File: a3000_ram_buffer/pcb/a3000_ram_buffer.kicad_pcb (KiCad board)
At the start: 2 copper layers, 167.6 x 43.2 mm, 29 parts

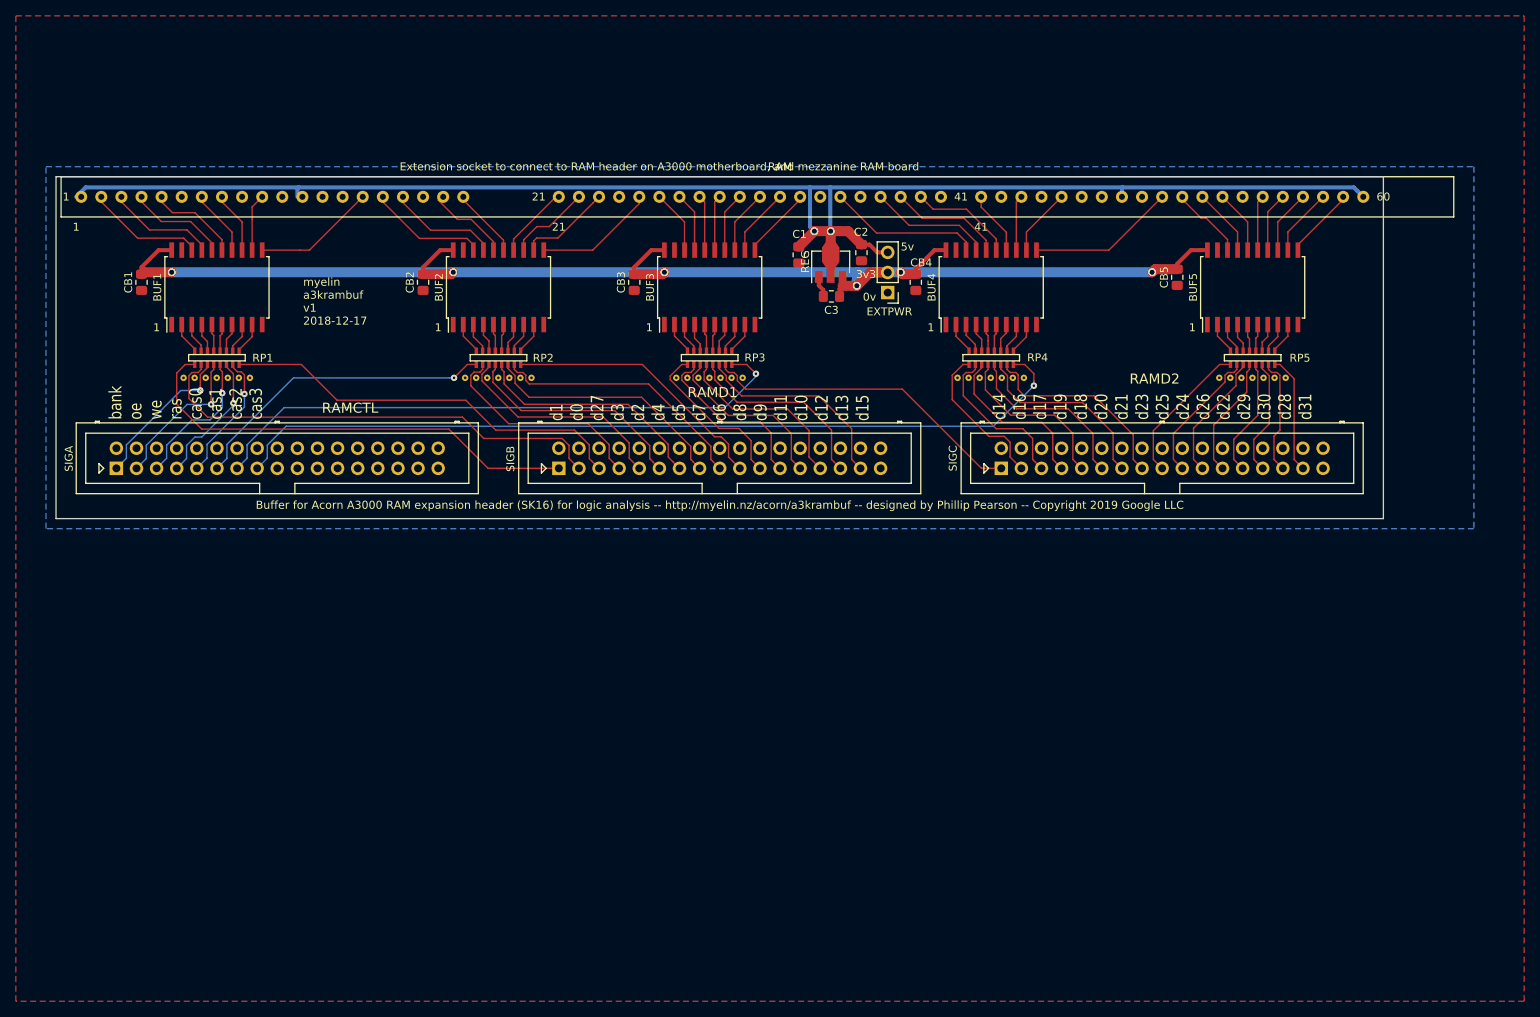
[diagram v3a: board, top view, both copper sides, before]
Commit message: added all other signal pins to ram buffer board -- as this plus a podule buffer will give quite a lot of visibility into what's going on in the system, even without the (expensive) MEMC clip.
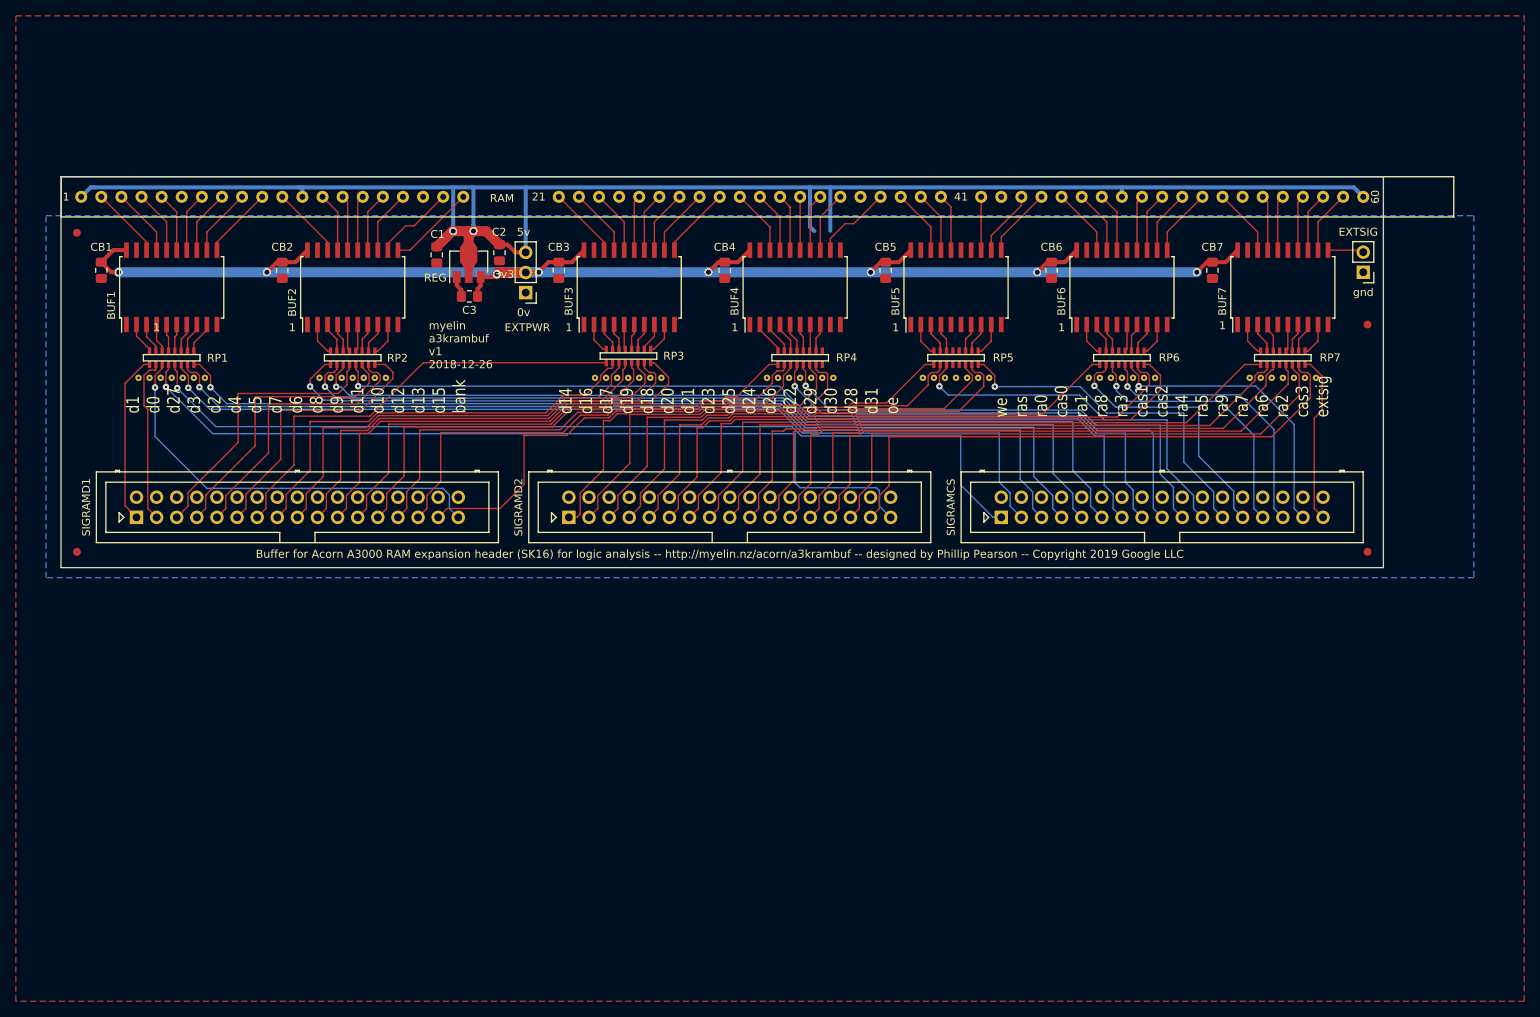
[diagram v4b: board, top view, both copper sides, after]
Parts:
- removed SIGA: signal header A, Connector_Multicomp:Multicomp_MC9A12-3434_2x17_P2.54mm_Vertical
- removed SIGB: signal header B, Connector_Multicomp:Multicomp_MC9A12-3434_2x17_P2.54mm_Vertical
- removed SIGC: signal header C, Connector_Multicomp:Multicomp_MC9A12-3434_2x17_P2.54mm_Vertical
- added BUF6: 74LVC245, Package_SO:SOIC-20W_7.5x12.8mm_P1.27mm, F.Cu at (170.2, 64.8)
- added BUF7: 74LVC245, Package_SO:SOIC-20W_7.5x12.8mm_P1.27mm, F.Cu at (190.5, 64.8)
- added CB6: 100n, Capacitor_SMD:C_0805_2012Metric_Pad1.15x1.40mm_HandSolder, F.Cu at (161.3, 62.6)
- added CB7: 100n, Capacitor_SMD:C_0805_2012Metric_Pad1.15x1.40mm_HandSolder, F.Cu at (181.6, 62.6)
- added EXTSIG: ext signal, Connector_PinHeader_2.54mm:PinHeader_1x02_P2.54mm_Vertical, F.Cu at (200.7, 62.9)
- added FID1: FIDUCIAL, Fiducial:Fiducial_1mm_Dia_2mm_Outer, F.Cu at (38.2, 57.9)
- added FID2: FIDUCIAL, Fiducial:Fiducial_1mm_Dia_2mm_Outer, F.Cu at (201.2, 69.5)
- added FID3: FIDUCIAL, Fiducial:Fiducial_1mm_Dia_2mm_Outer, F.Cu at (38.2, 98.2)
- added FID4: FIDUCIAL, Fiducial:Fiducial_1mm_Dia_2mm_Outer, F.Cu at (201.2, 98.2)
- added RP6: resistor pack, myelin-kicad:bourns_cat16_j8_resistor_array, F.Cu at (170.2, 73.7)
- added RP7: resistor pack, myelin-kicad:bourns_cat16_j8_resistor_array, F.Cu at (190.5, 73.7)
- added SIGRAMCS: signal header RAMCS, Connector_Multicomp:Multicomp_MC9A12-3434_2x17_P2.54mm_Vertical, F.Cu at (154.9, 93.8)
- added SIGRAMD1: signal header RAMD1, Connector_Multicomp:Multicomp_MC9A12-3434_2x17_P2.54mm_Vertical, F.Cu at (45.7, 93.8)
- added SIGRAMD2: signal header RAMD2, Connector_Multicomp:Multicomp_MC9A12-3434_2x17_P2.54mm_Vertical, F.Cu at (100.3, 93.8)
- added STAPLE6: via array, myelin-kicad:via_array_1x7_55mil, F.Cu at (169.5, 76.2)
- added STAPLE7: via array, myelin-kicad:via_array_1x7_55mil, F.Cu at (191.2, 76.2)
- moved EXTPWR 45.7 mm to (94.9, 65.4)
- moved REG 45.7 mm to (87.7, 62.0)
- moved C1 45.7 mm to (83.6, 60.7)
- moved C2 45.7 mm to (91.6, 60.4)
- moved C3 45.7 mm to (87.8, 65.9)
- moved BUF5 37.5 mm to (149.2, 64.8)
- moved RP5 37.5 mm to (149.2, 73.7)
- moved STAPLE5 37.4 mm to (149.9, 76.2)
- moved CB5 36.8 mm to (140.3, 62.6)
- moved BUF4 24.8 mm to (128.9, 64.8)
- moved CB4 24.2 mm to (120.0, 62.6)
- moved RP4 24.1 mm to (129.5, 73.7)
- moved STAPLE4 24.1 mm to (130.2, 76.2)
- moved BUF2 18.4 mm to (73.0, 64.8)
- moved RP2 18.4 mm to (73.0, 73.7)
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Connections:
- net ram_D26_buf renamed ram_RA5_buf
- net ram_D31_buf renamed ram_RA9_buf
- BUF1 pad 11: ram_D27 -> ram_nCAS0
- BUF1 pad 12: ram_nCAS0 -> ram_RA0
- BUF1 pad 8: ram_nCAS0_buf -> ram_RA0_buf
- BUF1 pad 9: ram_D27_buf -> ram_nCAS0_buf
- BUF2 pad 11: ram_D8 -> ram_D4
- BUF2 pad 12: ram_D6 -> ram_D2
- BUF2 pad 13: ram_D7 -> ram_D3
- BUF2 pad 14: ram_D5 -> ram_nCAS1
- BUF2 pad 15: ram_D4 -> ram_D27
- BUF2 pad 16: ram_D2 -> ram_RA3
- BUF2 pad 17: ram_D3 -> ram_RA8
- BUF2 pad 18: ram_nCAS1 -> ram_RA1
- BUF2 pad 2: ram_nCAS1_buf -> ram_RA1_buf
- BUF2 pad 3: ram_D3_buf -> ram_RA8_buf
- BUF2 pad 4: ram_D2_buf -> ram_RA3_buf
- BUF2 pad 5: ram_D4_buf -> ram_D27_buf
- BUF2 pad 6: ram_D5_buf -> ram_nCAS1_buf
- BUF2 pad 7: ram_D7_buf -> ram_D3_buf
- BUF2 pad 8: ram_D6_buf -> ram_D2_buf
- BUF2 pad 9: ram_D8_buf -> ram_D4_buf
- BUF3 pad 11: ram_nCAS2 -> ram_D12
- BUF3 pad 12: ram_D14 -> ram_D10
- BUF3 pad 13: ram_D15 -> ram_D11
- BUF3 pad 14: ram_D13 -> ram_D9
- BUF3 pad 15: ram_D12 -> ram_D8
- BUF3 pad 16: ram_D10 -> ram_D6
- BUF3 pad 17: ram_D11 -> ram_D7
- BUF3 pad 18: ram_D9 -> ram_D5
- BUF3 pad 2: ram_D9_buf -> ram_D5_buf
- BUF3 pad 3: ram_D11_buf -> ram_D7_buf
- BUF3 pad 4: ram_D10_buf -> ram_D6_buf
- BUF3 pad 5: ram_D12_buf -> ram_D8_buf
- BUF3 pad 6: ram_D13_buf -> ram_D9_buf
- BUF3 pad 7: ram_D15_buf -> ram_D11_buf
- BUF3 pad 8: ram_D14_buf -> ram_D10_buf
- BUF3 pad 9: ram_nCAS2_buf -> ram_D12_buf
- BUF4 pad 11: ram_nCAS3 -> GND
- BUF4 pad 12: ram_D23 -> ram_D17
- BUF4 pad 13: ram_D21 -> ram_D16
- BUF4 pad 14: ram_D20 -> ram_RA4
- BUF4 pad 15: ram_D18 -> ram_nCAS2
- BUF4 pad 16: ram_D19 -> ram_D14
- BUF4 pad 17: ram_D17 -> ram_D15
- BUF4 pad 18: ram_D16 -> ram_D13
- BUF4 pad 2: ram_D16_buf -> ram_D13_buf
- BUF4 pad 3: ram_D17_buf -> ram_D15_buf
- BUF4 pad 4: ram_D19_buf -> ram_D14_buf
- BUF4 pad 5: ram_D18_buf -> ram_nCAS2_buf
- BUF4 pad 6: ram_D20_buf -> ram_RA4_buf
- BUF4 pad 7: ram_D21_buf -> ram_D16_buf
- BUF4 pad 8: ram_D23_buf -> ram_D17_buf
- BUF4 pad 9: ram_nCAS3_buf -> (no net)
- BUF5 pad 11: ram_D31 -> ram_RA9
- BUF5 pad 12: ram_D28 -> ram_D21
- BUF5 pad 13: ram_D30 -> ram_D20
- BUF5 pad 14: ram_D29 -> GND
- BUF5 pad 15: ram_D22 -> GND
- BUF5 pad 16: ram_D26 -> ram_RA5
- BUF5 pad 17: ram_D24 -> ram_D18
- BUF5 pad 18: ram_D25 -> ram_D19
- BUF5 pad 2: ram_D25_buf -> ram_D19_buf
- BUF5 pad 3: ram_D24_buf -> ram_D18_buf
- BUF5 pad 5: ram_D22_buf -> (no net)
- BUF5 pad 6: ram_D29_buf -> (no net)
- BUF5 pad 7: ram_D30_buf -> ram_D20_buf
- BUF5 pad 8: ram_D28_buf -> ram_D21_buf
- RAM pad 11: (no net) -> ram_RA1
- RAM pad 13: (no net) -> ram_RA8
- RAM pad 14: (no net) -> ram_RA3
- RAM pad 34: (no net) -> ram_RA4
- RAM pad 40: (no net) -> ram_RA5
- RAM pad 44: (no net) -> ram_RA9
- RAM pad 46: (no net) -> ram_RA7
- RAM pad 47: (no net) -> ram_RA6
- RAM pad 49: (no net) -> ram_RA2
- RAM pad 9: (no net) -> ram_RA0
- RP1 pad 7A: ram_nCAS0_term -> ram_RA0_term
- RP1 pad 7B: ram_nCAS0_buf -> ram_RA0_buf
- RP1 pad 8A: ram_D27_term -> ram_nCAS0_term
- RP1 pad 8B: ram_D27_buf -> ram_nCAS0_buf
- RP2 pad 1A: ram_nCAS1_term -> ram_RA1_term
- RP2 pad 1B: ram_nCAS1_buf -> ram_RA1_buf
- RP2 pad 2A: ram_D3_term -> ram_RA8_term
- RP2 pad 2B: ram_D3_buf -> ram_RA8_buf
- RP2 pad 3A: ram_D2_term -> ram_RA3_term
- RP2 pad 3B: ram_D2_buf -> ram_RA3_buf
- RP2 pad 4A: ram_D4_term -> ram_D27_term
- RP2 pad 4B: ram_D4_buf -> ram_D27_buf
- RP2 pad 5A: ram_D5_term -> ram_nCAS1_term
- RP2 pad 5B: ram_D5_buf -> ram_nCAS1_buf
- RP2 pad 6A: ram_D7_term -> ram_D3_term
- RP2 pad 6B: ram_D7_buf -> ram_D3_buf
- RP2 pad 7A: ram_D6_term -> ram_D2_term
- RP2 pad 7B: ram_D6_buf -> ram_D2_buf
- RP2 pad 8A: ram_D8_term -> ram_D4_term
- RP2 pad 8B: ram_D8_buf -> ram_D4_buf
- RP3 pad 1A: ram_D9_term -> ram_D5_term
- RP3 pad 1B: ram_D9_buf -> ram_D5_buf
- RP3 pad 2A: ram_D11_term -> ram_D7_term
- RP3 pad 2B: ram_D11_buf -> ram_D7_buf
- RP3 pad 3A: ram_D10_term -> ram_D6_term
- RP3 pad 3B: ram_D10_buf -> ram_D6_buf
- RP3 pad 4A: ram_D12_term -> ram_D8_term
- RP3 pad 4B: ram_D12_buf -> ram_D8_buf
- RP3 pad 5A: ram_D13_term -> ram_D9_term
- RP3 pad 5B: ram_D13_buf -> ram_D9_buf
- RP3 pad 6A: ram_D15_term -> ram_D11_term
- RP3 pad 6B: ram_D15_buf -> ram_D11_buf
- RP3 pad 7A: ram_D14_term -> ram_D10_term
- RP3 pad 7B: ram_D14_buf -> ram_D10_buf
- RP3 pad 8A: ram_nCAS2_term -> ram_D12_term
- RP3 pad 8B: ram_nCAS2_buf -> ram_D12_buf
- RP4 pad 1A: ram_D16_term -> ram_D13_term
- RP4 pad 1B: ram_D16_buf -> ram_D13_buf
- RP4 pad 2A: ram_D17_term -> ram_D15_term
- RP4 pad 2B: ram_D17_buf -> ram_D15_buf
- RP4 pad 3A: ram_D19_term -> ram_D14_term
- RP4 pad 3B: ram_D19_buf -> ram_D14_buf
- RP4 pad 4A: ram_D18_term -> ram_nCAS2_term
- RP4 pad 4B: ram_D18_buf -> ram_nCAS2_buf
- RP4 pad 5A: ram_D20_term -> ram_RA4_term
- RP4 pad 5B: ram_D20_buf -> ram_RA4_buf
- RP4 pad 6A: ram_D21_term -> ram_D16_term
- RP4 pad 6B: ram_D21_buf -> ram_D16_buf
- RP4 pad 7A: ram_D23_term -> ram_D17_term
- RP4 pad 7B: ram_D23_buf -> ram_D17_buf
- RP4 pad 8A: ram_nCAS3_term -> GND
- RP4 pad 8B: ram_nCAS3_buf -> GND
- RP5 pad 1A: ram_D25_term -> ram_D19_term
- RP5 pad 1B: ram_D25_buf -> ram_D19_buf
- RP5 pad 2A: ram_D24_term -> ram_D18_term
- RP5 pad 2B: ram_D24_buf -> ram_D18_buf
- RP5 pad 3A: ram_D26_term -> ram_RA5_term
- RP5 pad 4A: ram_D22_term -> GND
- RP5 pad 4B: ram_D22_buf -> GND
- RP5 pad 5A: ram_D29_term -> GND
- RP5 pad 5B: ram_D29_buf -> GND
- RP5 pad 6A: ram_D30_term -> ram_D20_term
- RP5 pad 6B: ram_D30_buf -> ram_D20_buf
- RP5 pad 7A: ram_D28_term -> ram_D21_term
- RP5 pad 7B: ram_D28_buf -> ram_D21_buf
- RP5 pad 8A: ram_D31_term -> ram_RA9_term
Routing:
- net ram_RA0_term: track 0.00 -> 121.9 mm, vias 0 -> 1
- net ram_RA3_term: track 0.00 -> 114.0 mm, vias 0 -> 1
- net ram_RA8_term: track 0.00 -> 113.7 mm, vias 0 -> 1
- net ram_RA1_term: track 0.00 -> 113.3 mm, vias 0 -> 1
- net ram_nCAS0_term: track 16.5 -> 123.1 mm
- net ram_nRAS_term: track 17.0 -> 119.9 mm
- net ram_nWR2_term: track 18.0 -> 117.6 mm
- net ram_nOE2_term: track 18.9 -> 106.1 mm
- net ram_nCAS1_term: track 39.2 -> 113.7 mm
- net ram_nCAS3_term: track 108.0 -> 37.0 mm
- net ram_RA4_term: track 0.00 -> 62.5 mm, vias 0 -> 1
- net ram_D26_term: track 16.2 -> 74.6 mm
- net ram_D22_term: track 15.5 -> 73.5 mm
- net ram_D29_term: track 14.9 -> 72.2 mm
- net ram_D30_term: track 14.8 -> 72.0 mm
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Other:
- board size 167.6 x 43.2 mm -> 167 x 49.4 mm
- board text added: "d1 d0 d27 d3 d2 d4 d5 d7 d6 d8 d9 d11 d10 d12 d13 d15 bank"
- board text added: "d14 d16 d17 d19 d18 d20 d21 d23 d25 d24 d26 d22 d29 d30 d28 d31 oe"
- board text added: "gnd"
- board text added: "myelin a3krambuf v1 2018-12-26"
- board text added: "we ras ra0 cas0 ra1 ra8 ra3 cas1 cas2 ra4 ra5 ra9 ra7 ra6 ra2 cas3 extsig"
- board text removed: "21"
- board text removed: "41"
- board text removed: "RAMCTL"
- board text removed: "RAMD1"
- board text removed: "RAMD2"
- board text removed: "bank oe we ras cas0 cas1 cas2 cas3"
- board text removed: "d1 d0 d27 d3 d2 d4 d5 d7 d6 d8 d9 d11 d10 d12 d13 d15"
- board text removed: "d14 d16 d17 d19 d18 d20 d21 d23 d25 d24 d26 d22 d29 d30 d28 d31"
- board text removed: "myelin a3krambuf v1 2018-12-17"

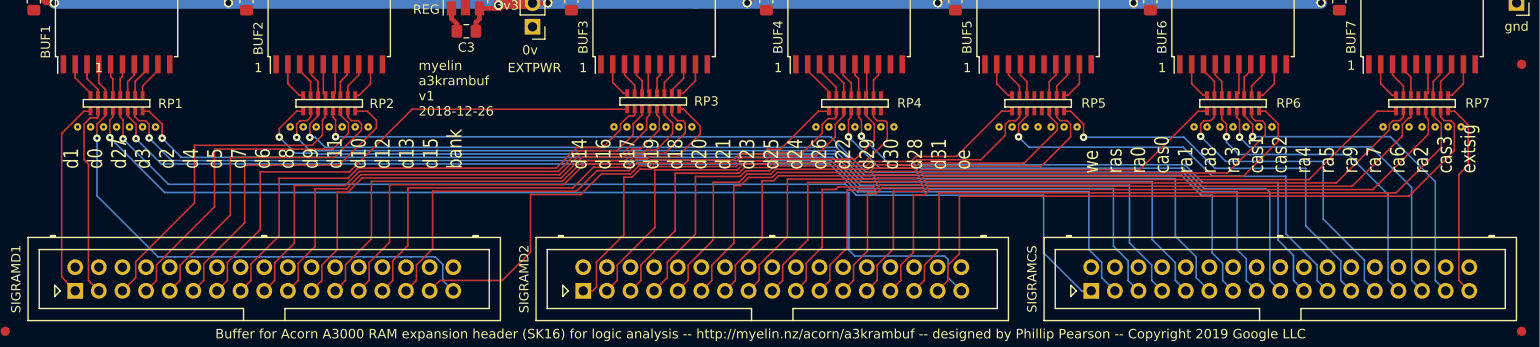
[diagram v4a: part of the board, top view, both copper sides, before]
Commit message: Tidied all terminated signals so all signals are separated by the ground plane
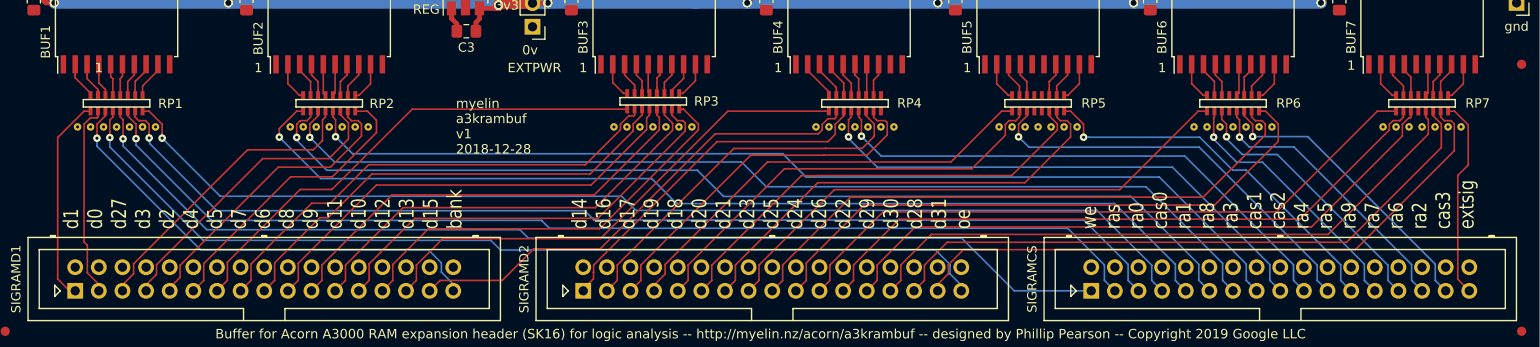
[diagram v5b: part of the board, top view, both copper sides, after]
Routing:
- net ram_RA7_term: track 34.2 -> 28.1 mm
- net ram_nCAS3_term: track 37.0 -> 31.8 mm
- net ram_RA2_term: track 35.2 -> 30.4 mm
- net ram_RA6_term: track 34.1 -> 29.4 mm
- net ram_nCAS2_term: track 61.7 -> 57.2 mm
- net ram_D12_term: track 49.9 -> 45.5 mm
- net ram_D14_term: track 42.3 -> 37.9 mm
- net ram_RA4_term: track 62.5 -> 58.2 mm
- net ram_nCAS1_term: track 113.7 -> 109.8 mm
- net ram_D17_term: track 43.1 -> 39.2 mm
- net ram_RA9_term: track 44.5 -> 40.7 mm
- net ram_D16_term: track 43.5 -> 39.7 mm
- net ram_D6_term: track 54.5 -> 50.6 mm
- net ram_D11_term: track 50.9 -> 47.0 mm
- net ram_D15_term: track 56.3 -> 52.4 mm
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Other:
- board text added: "myelin a3krambuf v1 2018-12-28"
- board text removed: "myelin a3krambuf v1 2018-12-26"
